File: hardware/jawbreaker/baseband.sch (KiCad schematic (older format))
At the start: 109 parts, among them P1 RX_SMA, P2 TX_SMA, P8 CLKIN, P9 CLKIN_JMP, T1 RX_BALUN, T2 TX_BALUN, U1 MAX5864, U2 MAX2837, U3 SI5351C, X1 GSG-XTAL4PIN

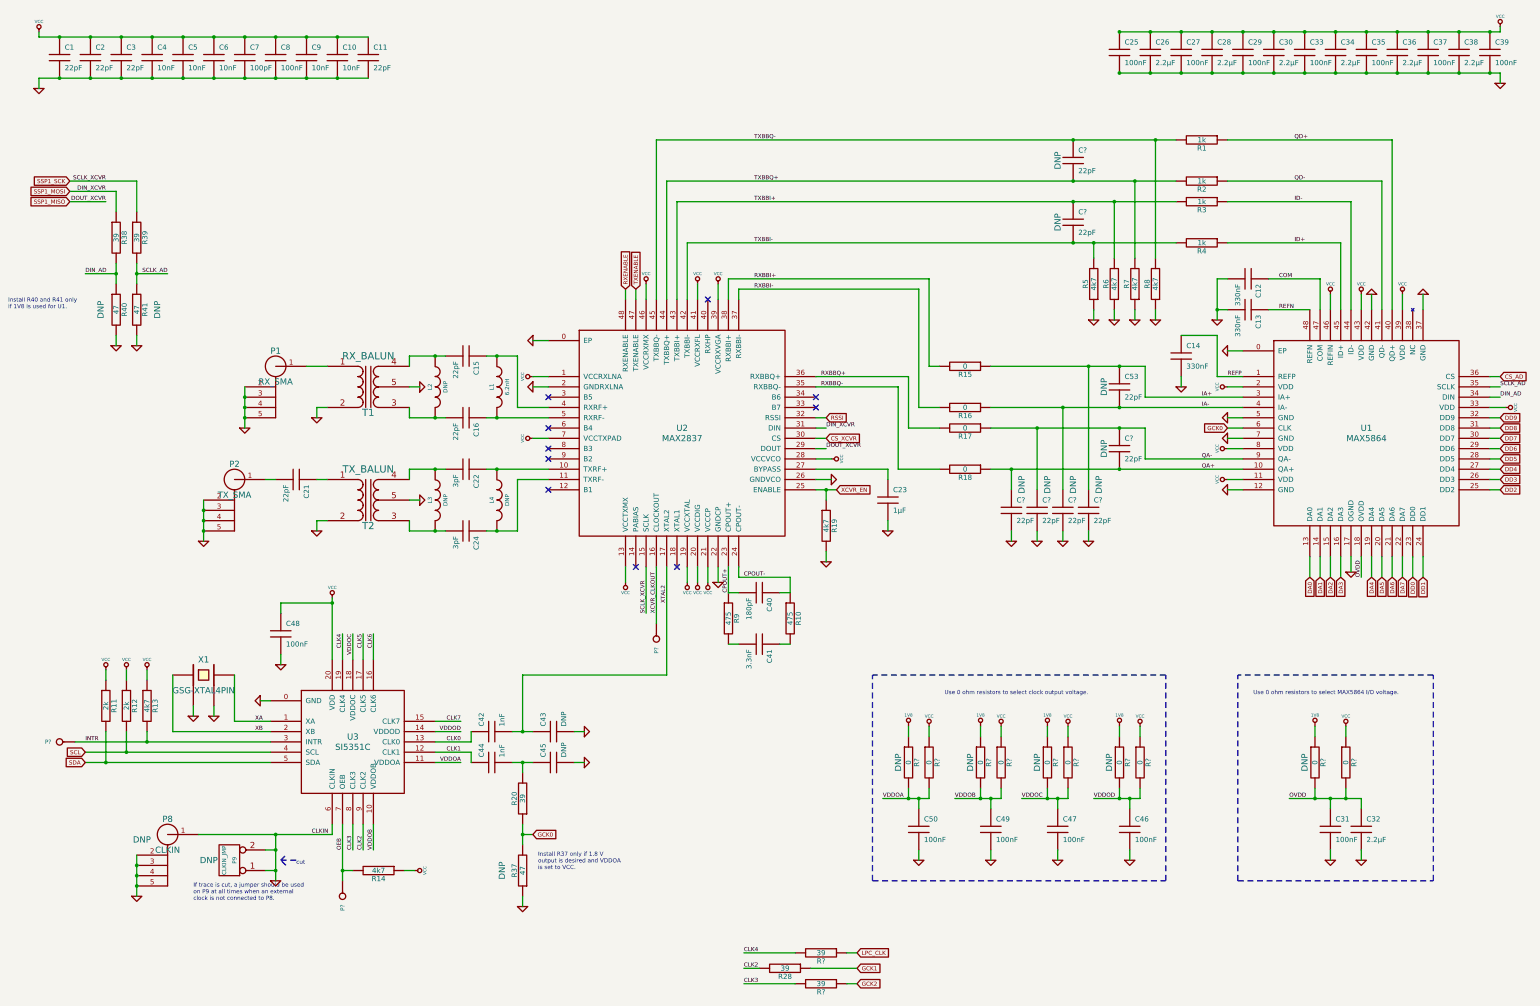
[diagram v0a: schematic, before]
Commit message: re-annotated everything
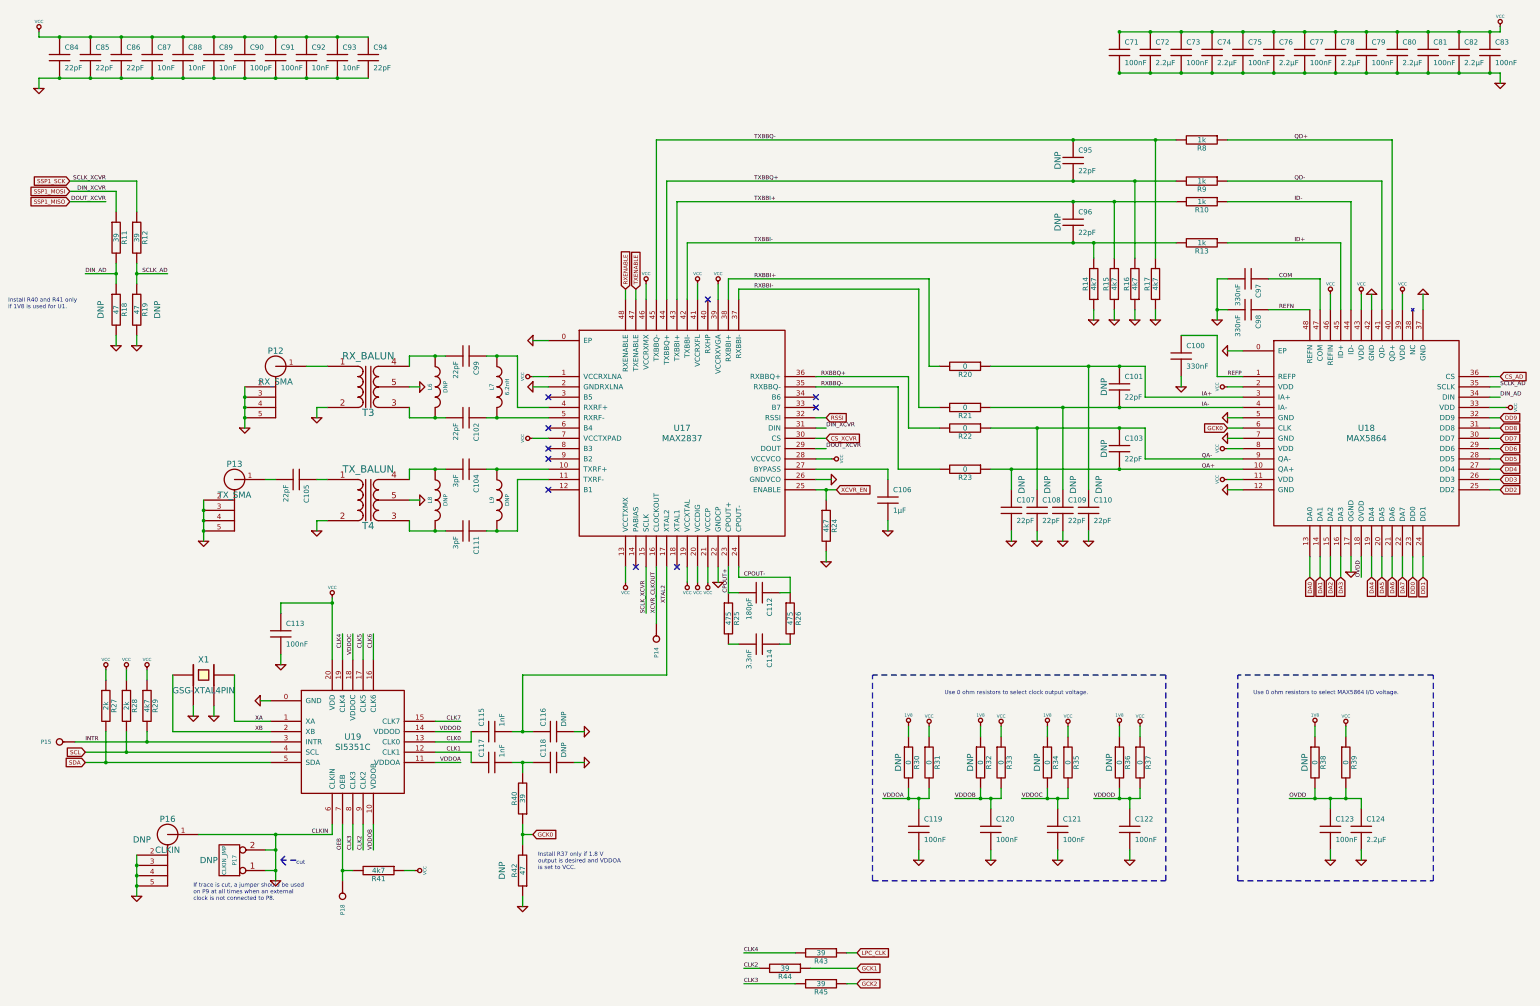
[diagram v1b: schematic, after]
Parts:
- gave numbers to parts that had none: 22
- renumbered C14 to C100, C53 to C101, C16 to C102, C22 to C104, C21 to C105, C23 to C106, C24 to C111, C40 to C112, C48 to C113, C41 to C114, C42 to C115, C43 to C116, C44 to C117, C45 to C118, C50 to C119, C49 to C120, C47 to C121, C46 to C122, C31 to C123, C32 to C124, C25 to C71, C26 to C72, C27 to C73, C28 to C74, C29 to C75, C30 to C76, C33 to C77, C34 to C78, C35 to C79, C36 to C80, C37 to C81, C38 to C82, C39 to C83, C1 to C84, C2 to C85, C3 to C86, C4 to C87, C5 to C88, C6 to C89, C7 to C90, C8 to C91, C9 to C92, C10 to C93, C11 to C94, C12 to C97, C13 to C98, C15 to C99, L2 to L6, L1 to L7, L3 to L8, L4 to L9, P1 to P12, P2 to P13, P8 to P16, P9 to P17, R3 to R10, R38 to R11, R39 to R12, R4 to R13, R5 to R14, R6 to R15, R7 to R16, R8 to R17, R40 to R18, R41 to R19, R15 to R20, R16 to R21, R17 to R22, R18 to R23, R19 to R24, R9 to R25, R10 to R26, R11 to R27, R12 to R28, R13 to R29, R20 to R40, R14 to R41, R37 to R42, R28 to R44, R1 to R8, R2 to R9, T1 to T3, T2 to T4, U2 to U17, U1 to U18, U3 to U19

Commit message: bom info, extra amp
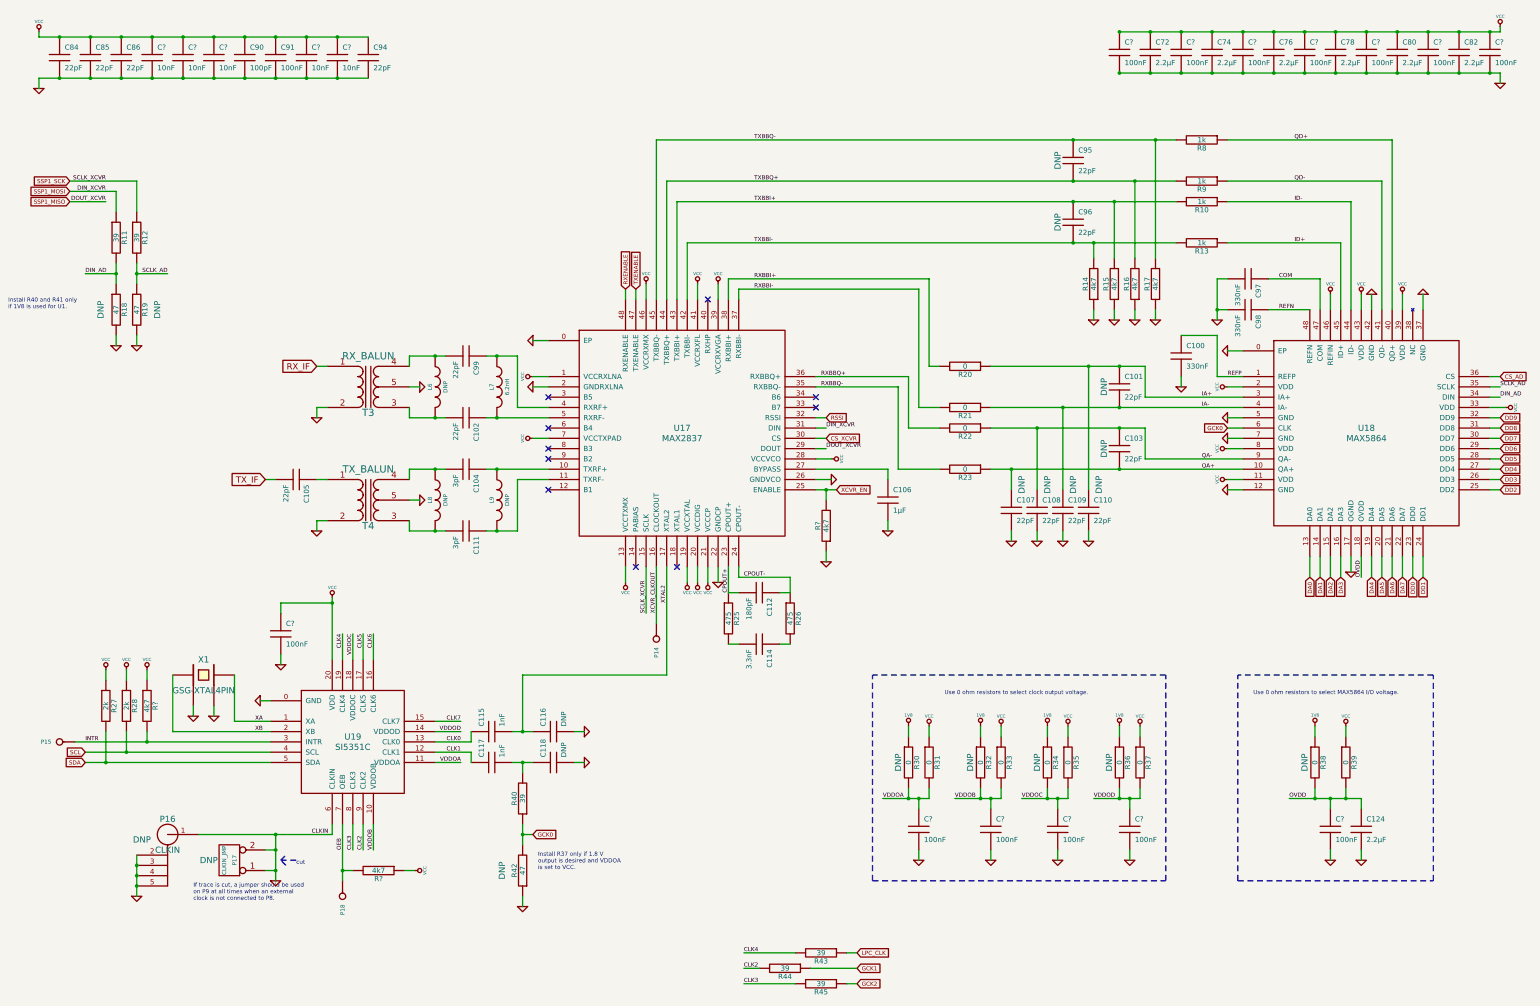
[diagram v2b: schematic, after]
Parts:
- removed C113, C119, C120, C121, C122, C123, C71, C73, C75, C77, C79, C81, C83: 100nF, symbol C
- removed C87, C88, C89, C92, C93: 10nF, symbol C
- removed P12: RX_SMA, symbol GSG-SMA-CONN
- removed P13: TX_SMA, symbol GSG-SMA-CONN
- removed R24, R29, R41: 4k7, symbol R
- added C? (x13): 100nF, symbol C
- added C? (x5): 10nF, symbol C
- added R? (x3): 4k7, symbol R
- P18: Note (none) -> DNP
- U17: Description (none) -> IC TXRX 2.3GHZ-2.7GHZ 48TQFN; Manufacturer (none) -> Maxim; Part Number (none) -> MAX2837ETM+T
- U18: Description (none) -> IC ANLG FRONT END 22MSPS 48-TQFN; Manufacturer (none) -> Maxim; Part Number (none) -> MAX5864ETM+T
- U19: Description (none) -> IC CLK GEN PLL BLANK CUST 20-QFN; Manufacturer (none) -> Silicon Laboratories Inc; Part Number (none) -> SI5351C-A-GM
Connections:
- net GND: now also C?.2, C?.2, C?.2, C?.2, C?.2, C?.2, C?.2, C?.2, C?.2, C?.2, C?.2, C?.2, C?.2, C?.2, C?.2, C?.2, C?.2, C?.2, R?.1
- net INTR: now also R?.2
- net OEB: now also R?.2
- net OVDD: now also C?.1
- net VCC: now also C?.1, C?.1, C?.1, C?.1, C?.1, C?.1, C?.1, C?.1, C?.1, C?.1, C?.1, C?.1, C?.1, R?.1, R?.1
- net VDDOA: now also C?.1
- net VDDOB: now also C?.1
- net VDDOC: now also C?.1
- net VDDOD: now also C?.1
- net XCVR_EN: now also R?.2
- net TX_IF: now reaches C105.2
- net RX_IF: now reaches T3.1 (S1)

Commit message: started replacing 0603s with 0402s
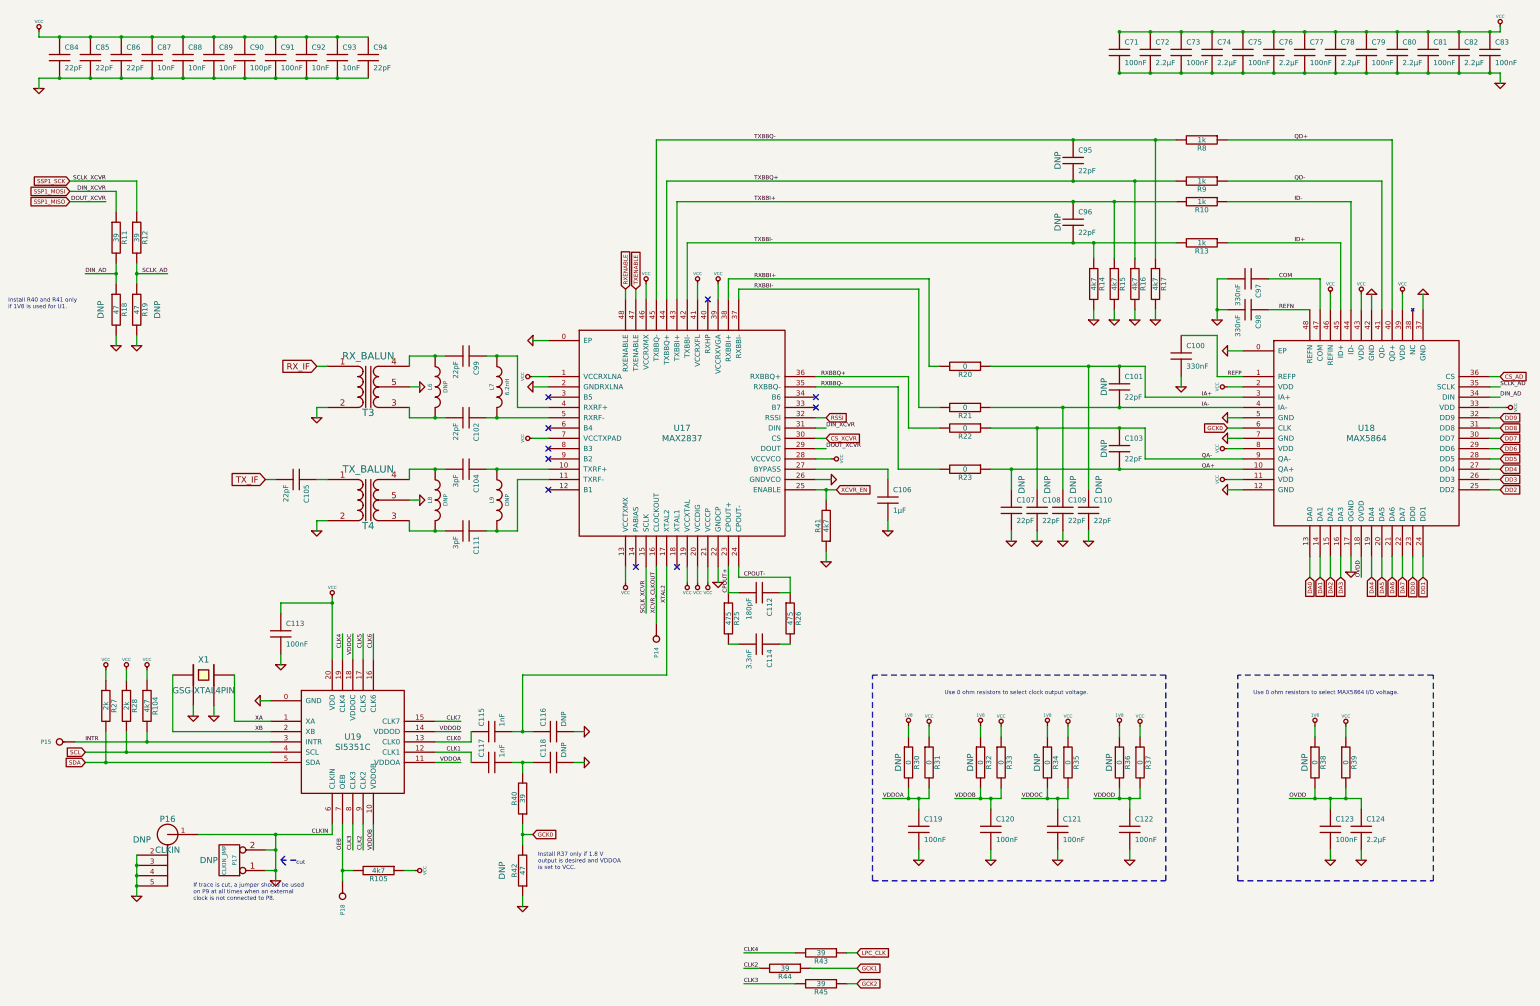
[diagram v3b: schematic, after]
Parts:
- C112: Description (none) -> CAP CER 180PF 50V 5% NP0 0402; Manufacturer (none) -> Murata; Part Number (none) -> GRM1555C1H181JA01D
- C91: Description (none) -> CAP CER 0.1UF 10V 10% X5R 0402; Manufacturer (none) -> Murata; Part Number (none) -> GRM155R61A104KA01D
- R14, R15, R16, R17: Description (none) -> RES 4.7K OHM 1/16W 5% 0402 SMD; Manufacturer (none) -> Stackpole; Part Number (none) -> RMCF0402JT4K70
- gave numbers to parts that had none: 21
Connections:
- net GND: now also R14.2, R15.2, R16.2, R17.2; no longer R14.1, R15.1, R16.1, R17.1
- net TXBBI+: now also R15.1; no longer R15.2
- net TXBBI-: now also R14.1; no longer R14.2
- net TXBBQ+: now also R16.1; no longer R16.2
- net TXBBQ-: now also R17.1; no longer R17.2

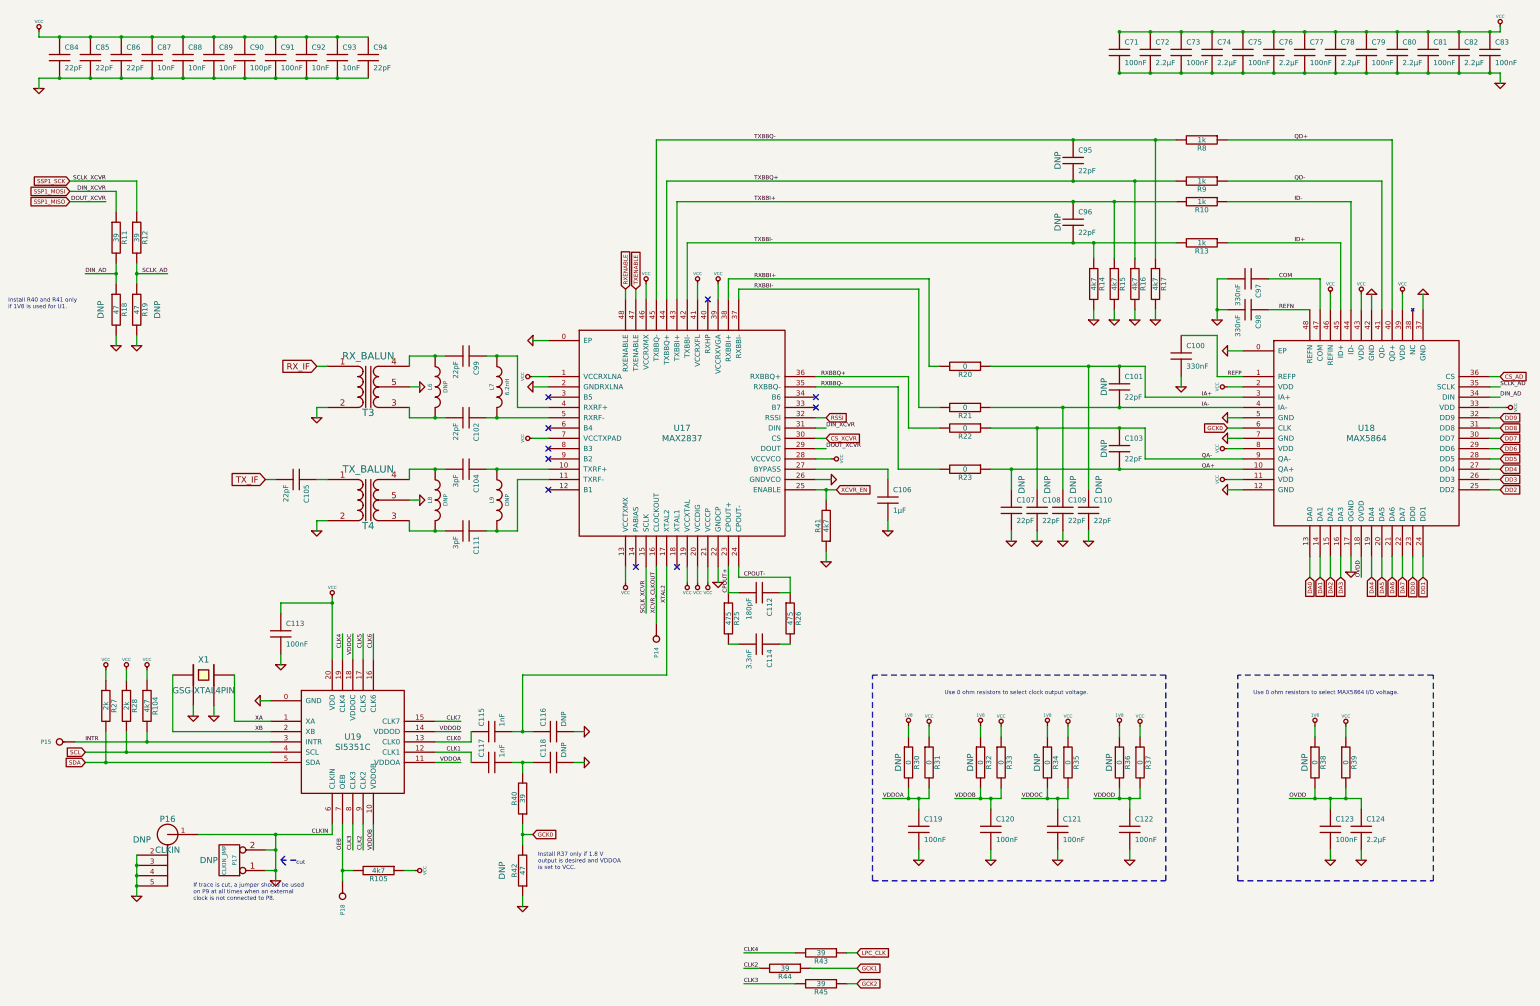
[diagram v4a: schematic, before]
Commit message: VCC filter components to be optionally replaced with LDO for analog supply
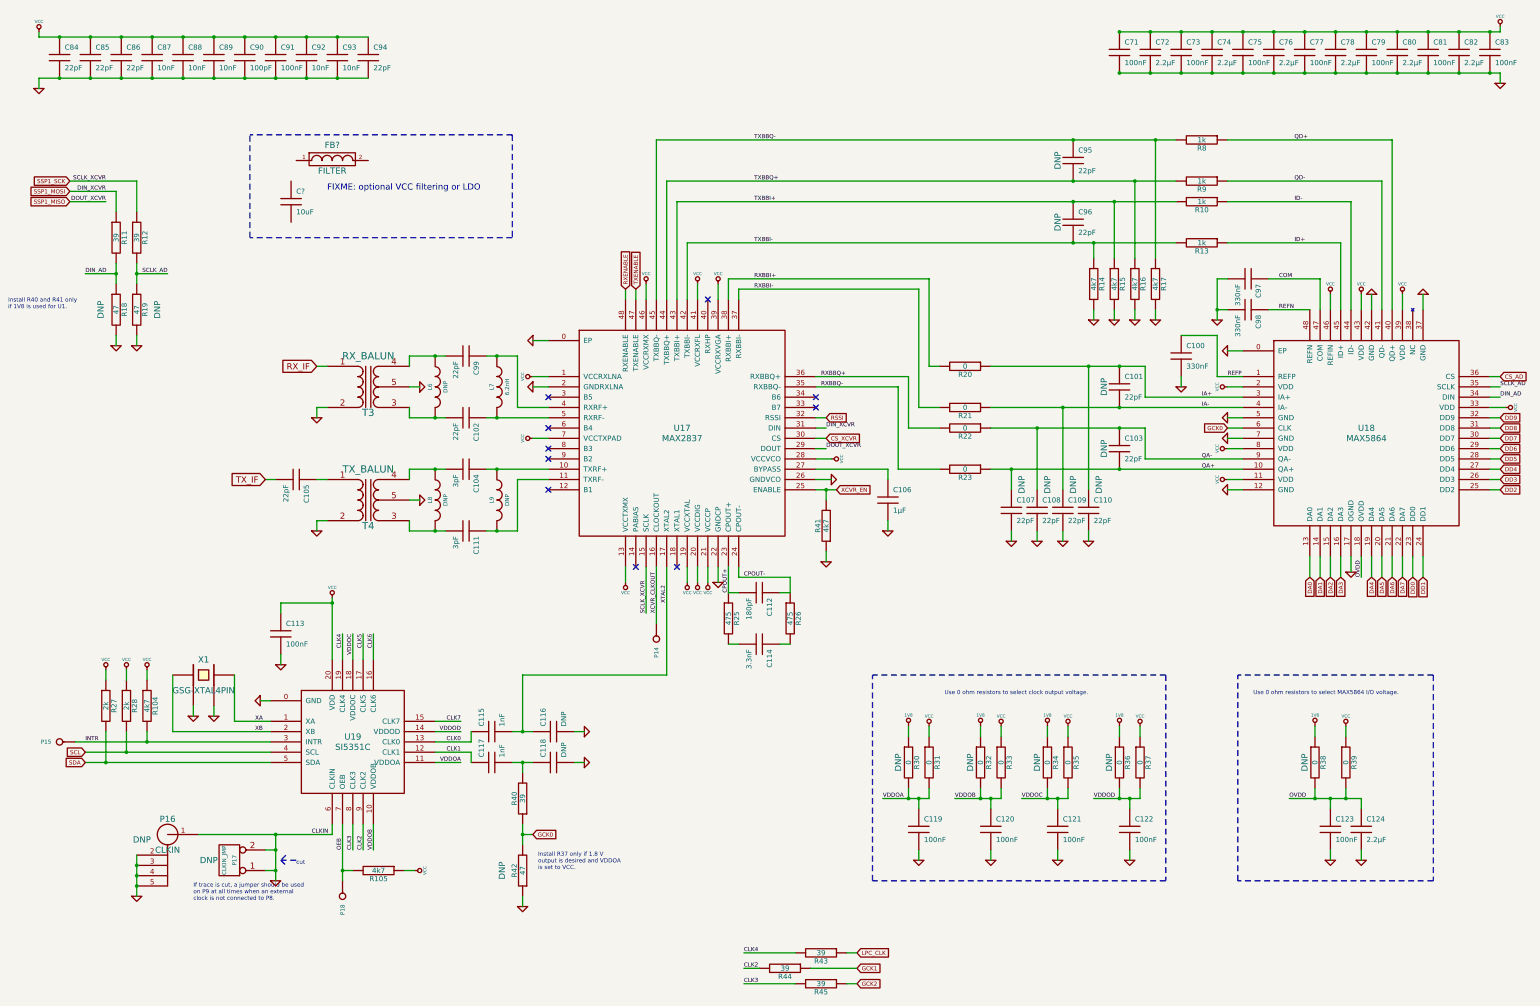
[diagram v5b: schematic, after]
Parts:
- added C?: 10uF, symbol C
- added FB?: FILTER, symbol FILTER
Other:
- note added: "FIXME: optional VCC filtering or LDO"
